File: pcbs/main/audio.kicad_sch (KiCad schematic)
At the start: 21 parts

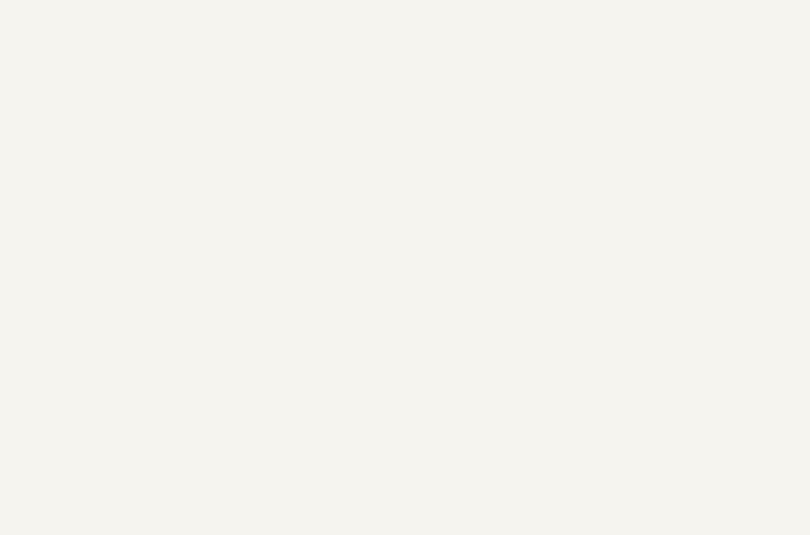
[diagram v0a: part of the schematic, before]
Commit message: Add power input stage, add EEPROM for GPIO autoconfiguration.
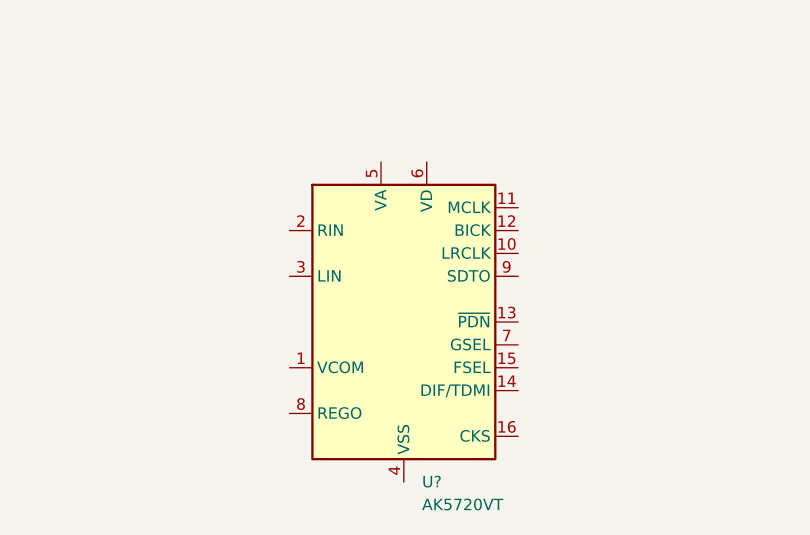
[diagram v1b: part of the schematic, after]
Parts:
- added U?: AK5720VT, Package_SO:TSSOP-16_4.4x5mm_P0.65mm, symbol Audio:AK5720VT
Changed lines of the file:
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@@
     (pin "2")
+  )
+  (symbol (lib_id "Audio:AK5720VT") (at 64.77 139.7 0) (unit 1)
+    (in_bom yes) (on_board yes) (fields_autoplaced)
+    (property "Reference" "U?" (id 0) (at 66.7894 157.48 0)
+      (effects (font (size 1.27 1.27)) (justify left))
+    )
+    (property "Value" "AK5720VT" (id 1) (at 66.7894 160.02 0)
+      (effects (font (size 1.27 1.27)) (justify left))
+    )
+    (property "Footprint" "Package_SO:TSSOP-16_4.4x5mm_P0.65mm" (id 2) (at 64.77 139.7 0)
+      (effects (font (size 1.27 1.27) italic) hide)
+    )
+    (property "Datasheet" "https://www.akm.com/akm/en/file/datasheet/AK5720VT.pdf" (id 3) (at 82.55 143.51 0)
+      (effects (font (size 1.27 1.27)) hide)
+    )
+    (pin "1")
+    (pin "10")
+    (pin "11")
+    (pin "12")
+    (pin "13")
+    (pin "14")
+    (pin "15")
+    (pin "16")
+    (pin "2")
+    (pin "3")
+    (pin "4")
+    (pin "5")
+    (pin "6")
+    (pin "7")
+    (pin "8")
+    (pin "9")
   )
   (symbol (lib_id "Device:R") (at 133.35 45.72 0) (unit 1)

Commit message: Add microphone ADC
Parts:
- removed U?: AK5720VT, Package_SO:TSSOP-16_4.4x5mm_P0.65mm, symbol Audio:AK5720VT
- added C? (x5): 10u, symbol Device:C
- added C? (x4): 0.1u, symbol Device:C
- added C?: 2.2u, symbol Device:C
- added MK?: Microphone, symbol Device:Microphone
- added R?: 2k2, symbol Device:R
- added U?: PCM1860, symbol pividbell_main_parts:PCM1860
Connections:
- net +3V3: now also C?.1, C?.1, C?.1, C?.1, C?.1, C?.1, U?.13 (DVDD), U?.14 (IOVDD), U?.8 (AVDD)
- net BCLK: now also U?.17 (BCK)
- net GND: now also C?.2, C?.2, C?.2, C?.2, C?.2, C?.2, C?.2, C?.2, C?.2, MK?.1 (-), U?.12 (DGND), U?.19 (INT), U?.20 (MD6), U?.21 (MD5), U?.22 (MD4), U?.23 (MD2), U?.24 (MD3), U?.25 (MD1), U?.26 (MD0), U?.7 (AGND)
- net LRCLK: now also U?.16 (LRCK)
- net MIC_DATA: now also U?.18 (DOUT)
- new net: C?.1, MK?.2 (+), R?.2
- new net: C?.2, U?.4 (VINR1/VIN2P)
- new net: C?.1, C?.1, U?.11 (LDO)
- new net: C?.1, U?.6 (VREF)
- new net: R?.1, U?.5 (Mic_Bias)
- no-connect marks 3 -> 13
